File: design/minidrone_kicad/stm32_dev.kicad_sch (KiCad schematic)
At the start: 31 parts, among them J10 Conn_01x20, J8 J-Link, J9 Conn_01x20, SW1 SW_DIP_x02, SW2 SW_Push, U1 LM1117MP-3.3, U2 STM32F103CBTx, Y1 8MHz, Y2 32,768KHz

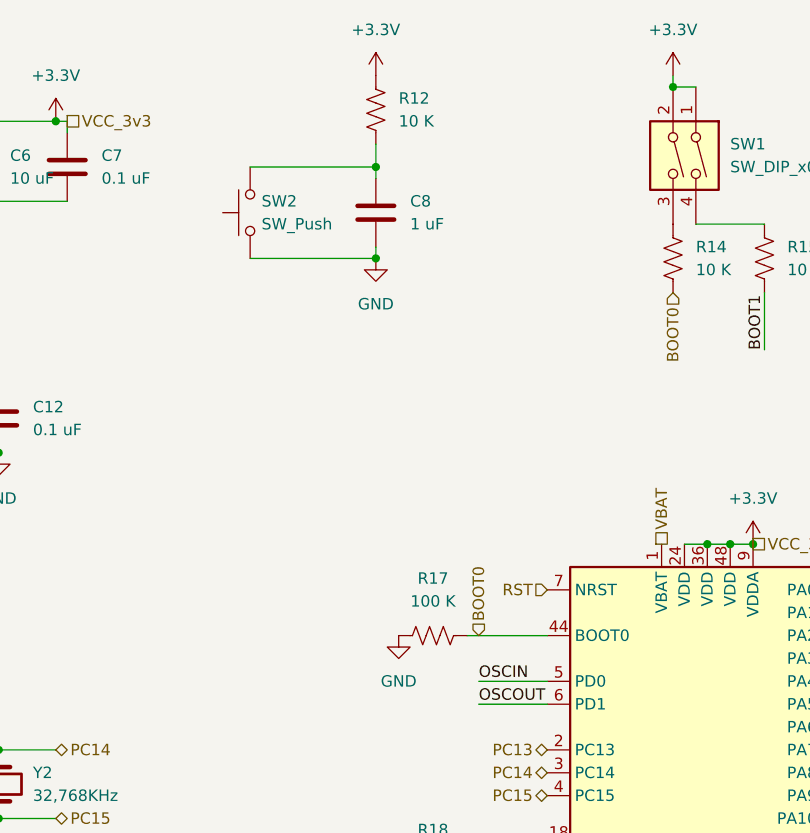
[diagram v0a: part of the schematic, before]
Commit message: fix(SCH/PCB): The reset button no function
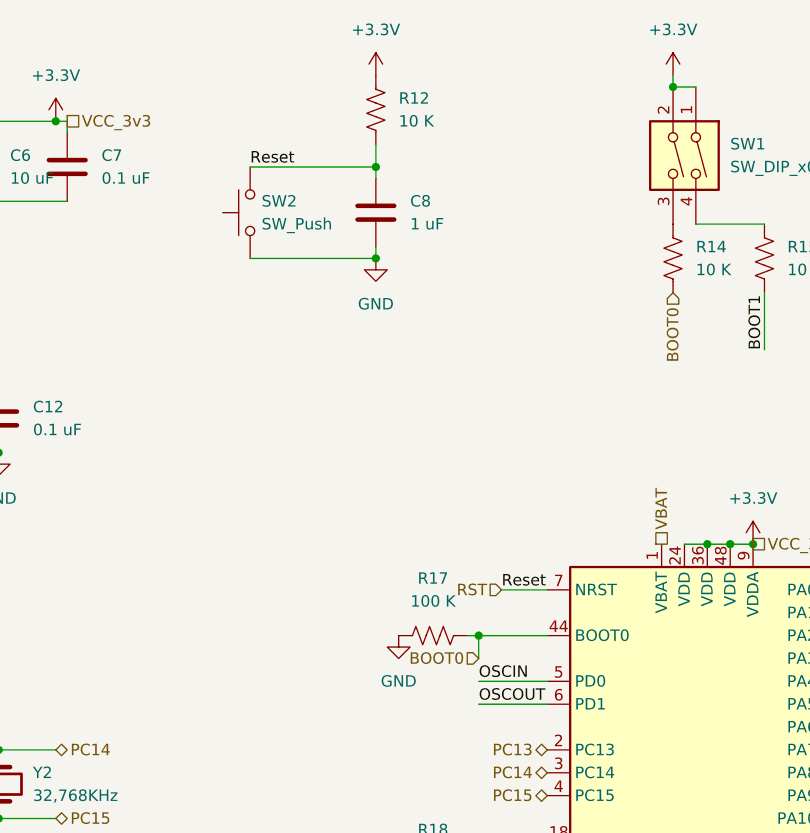
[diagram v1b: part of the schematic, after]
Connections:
- net RST: now also C8.1, R12.2, SW2.2
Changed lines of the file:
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@@
+	)
+	(junction
+		(at 124.46 83.82)
+		(diameter 0)
+		(color 0 0 0 0)
 	)
 	(junction
@@
 	(wire
 		(pts
+			(xy 124.46 83.82) (xy 132.08 83.82)
+		)
+		(stroke
+			(width 0)
+			(type default)
+		)
+	)
+	(wire
+		(pts
 			(xy 43.18 63.5) (xy 57.15 63.5)
 		)
@@
 	(wire
 		(pts
-			(xy 123.19 83.82) (xy 132.08 83.82)
+			(xy 123.19 83.82) (xy 124.46 83.82)
+		)
+		(stroke
+			(width 0)
+			(type default)
+		)
+	)
+	(wire
+		(pts
+			(xy 127 78.74) (xy 132.08 78.74)
 		)
 		(stroke
@@
 		(pts
 			(xy 57.15 55.88) (xy 71.12 55.88)
+		)
+		(stroke
+			(width 0)
+			(type default)
+		)
+	)
+	(wire
+		(pts
+			(xy 124.46 86.36) (xy 124.46 83.82)
 		)
 		(stroke
@@
 	(label "OSCOUT"
 		(at 41.91 104.14 0)
+		(fields_autoplaced yes)
+		(effects
+			(font
+				(size 1.27 1.27)
+			)
+			(justify left bottom)
+		)
+	)
+	(label "Reset"
+		(at 127 78.74 0)
+		(fields_autoplaced yes)
+		(effects
+			(font
+				(size 1.27 1.27)
+			)
+			(justify left bottom)
+		)
+	)
+	(label "Reset"
+		(at 99.06 31.75 0)
 		(fields_autoplaced yes)
 		(effects
@@
 	(hierarchical_label "BOOT0"
 		(shape input)
-		(at 124.46 83.82 90)
-		(fields_autoplaced yes)
-		(effects
-			(font
-				(size 1.27 1.27)
-			)
-			(justify left)
+		(at 124.46 86.36 180)
+		(fields_autoplaced yes)
+		(effects
+			(font
+				(size 1.27 1.27)
+			)
+			(justify right)
 		)
 	)
@@
 		)
 	)
+	(hierarchical_label "RST"
+		(shape input)
+		(at 127 78.74 180)
+		(fields_autoplaced yes)
+		(effects
+			(font
+				(size 1.27 1.27)
+			)
+			(justify right)
+		)
+	)
 	(hierarchical_label "PA15"
 		(shape bidirectional)
@@
 		(fields_autoplaced yes)
 		(effects
-			(font
-				(size 1.27 1.27)
-			)
-			(justify right)
-		)
-	)
-	(hierarchical_label "RST"
-		(shape input)
-		(at 132.08 78.74 180)
-		(fields_autoplaced yes)
-		(effects
